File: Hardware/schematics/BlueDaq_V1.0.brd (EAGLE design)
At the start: 67 x 72 mm, 72 parts, among them IC1 MEGA8-AI, Q1 MMBT2222, Q2 MMBT2222, Q3 MMBT2222, Q4 MMBT2222, U1 MCP73831, U2 TPS61200, U3 BME280, U4 MIC5225-3.3, U5 MIC5219 5V, X1 USB-MICROB, X2 3.5mm, X4 3.5mm, Y1 16 mhz

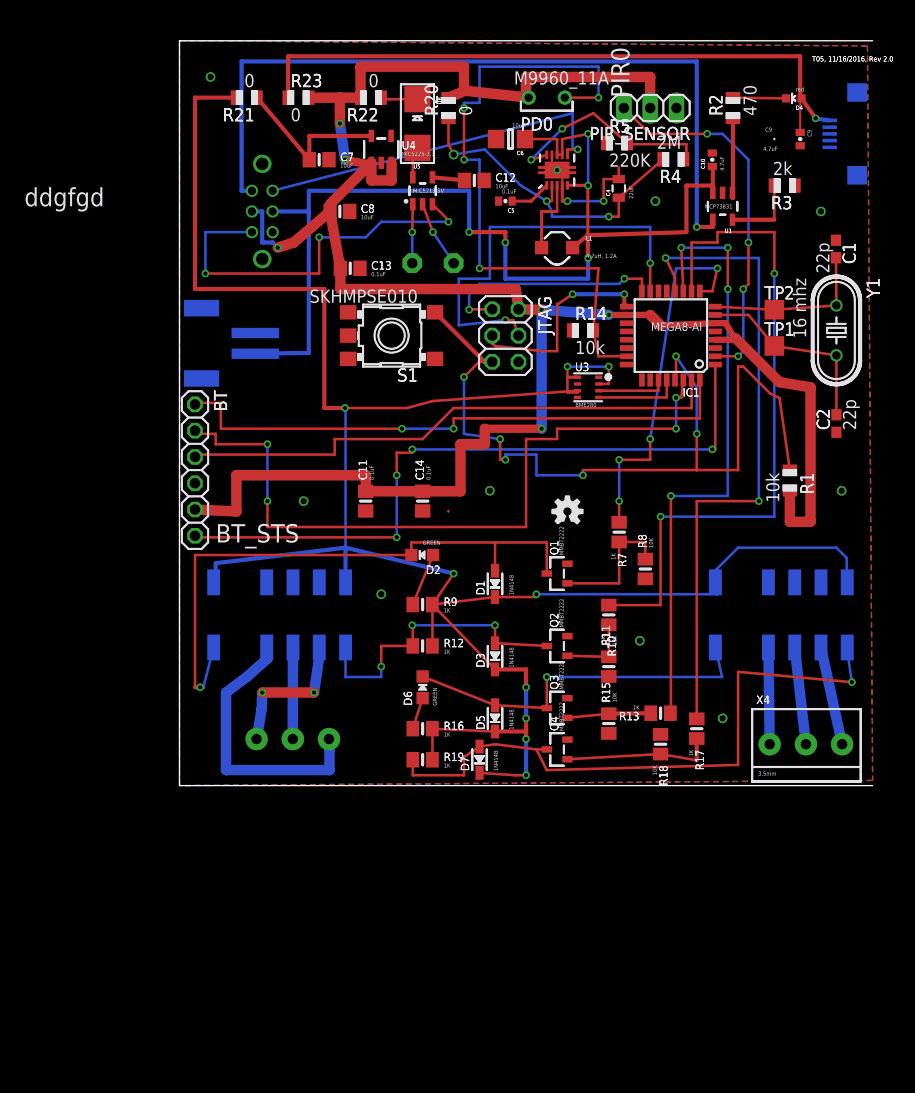
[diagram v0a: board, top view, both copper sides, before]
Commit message: cleaned up traces a little
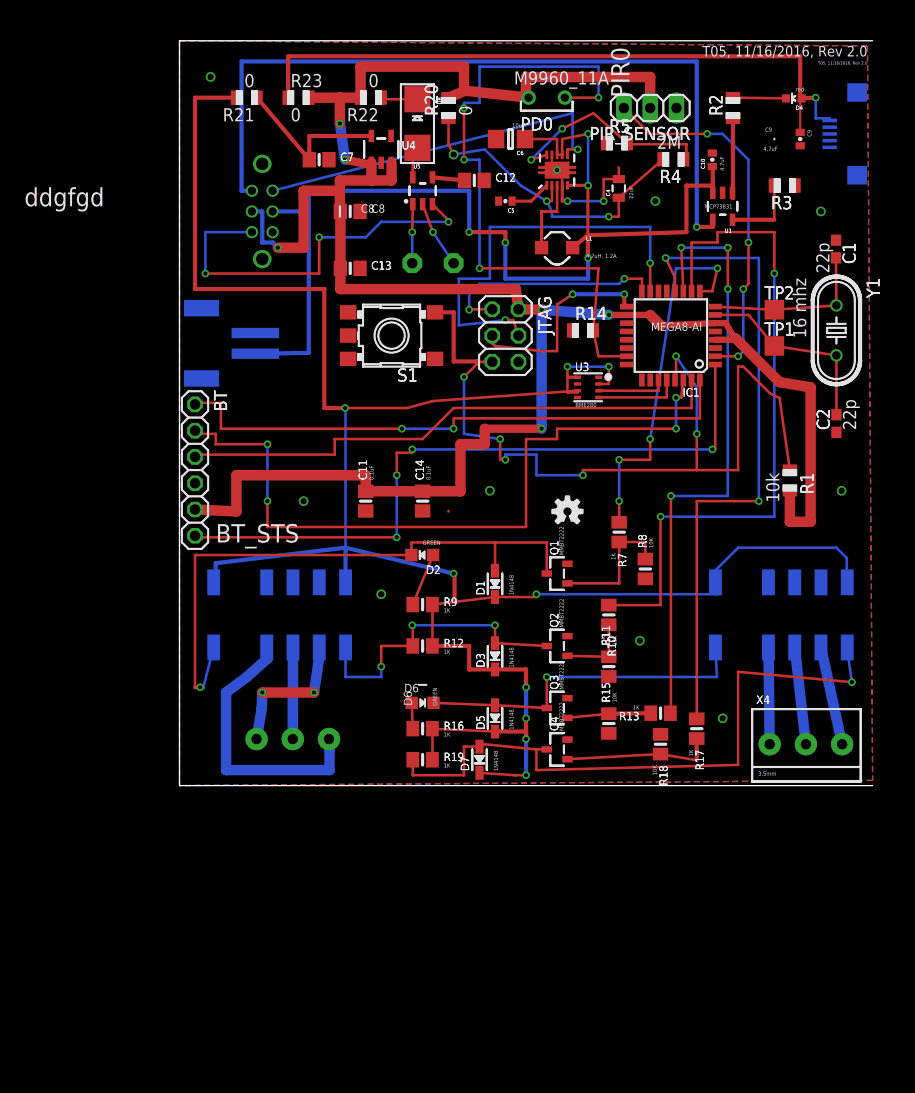
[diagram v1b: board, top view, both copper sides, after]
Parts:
- moved D6 1.50 mm to (23.0, 8.00), turned to 270 degrees
- moved C8 1.00 mm to (16.0, 55.5)
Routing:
- net VCC: track 212.1 -> 217.0 mm
- net RESET_PIN: track 84.0 -> 86.3 mm
- net N$7: track 35.4 -> 33.3 mm
- net N$12: track 60.8 -> 62.3 mm
- net 3.3V: track 218.8 -> 217.7 mm
- net N$23: track 64.7 -> 65.9 mm
- net N$9: track 3.10 -> 2.50 mm
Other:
- board text removed: "220K"
- board text removed: "2k"
- board text removed: "470"
- board text removed: "MIC5219 5V"
- board text removed: "MIC5225-3.3"
- board text removed: "R21"
- board text removed: "R22"
- board text removed: "R23"
- board text removed: "SKHMPSE010"

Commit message: lots of changes
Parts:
- removed S2: (no value), SparkFun-Electromechanical:EG2211
- added C15: 10uF, microbuilder:0805-NO@1
- added C3: 0.1uF, microbuilder:0805-NO@1
- added D10: (no value), adafruit:SMADIODE
- added R6: 4.7k, adafruit:R0805
- C12: value 10uF -> .1uF
- C13: value 0.1uF -> 10uF
- R23: value 0 -> 4.7k
- R4: value 2M -> 1.7M
- R5: value 220K -> 180K
- moved R23 90.5 mm to (-14.0, -20.5)
- moved C13 80.3 mm to (-14.0, -24.5)
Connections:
- removed net EN_5V: S2.P1-TB, U5.3
- removed net EN_BC: S2.P2-TA, U2.6
- removed net V_CHRG: S2.P1-TA, U1.4
- new net N$20: D10.A, R20.2
- new net N$36: C11.2, IC1.20
- net 3.3V: now also R23.2, R6.2
- net GND: now also C15.2, C3.1; no longer C13.2
- net N$15: now also C13.1, U5.3
- net N$16: now also C13.2
- net N$23: now also U1.4; no longer R23.1
- net N$5: now also C15.1
- net SCL: now also R6.1
- net SDA: now also R23.1
- net VBATT: now also U2.6; no longer S2.P2
- net VCC: now also C3.2, D10.C; no longer C11.2, C13.1, R20.2, R23.2, S2.P1
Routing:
- net V_CHRG: track 75.7 -> 0.00 mm, vias 1 -> 0
- net EN_5V: track 38.5 -> 0.00 mm, vias 3 -> 0
- net EN_BC: track 35.5 -> 0.00 mm, vias 1 -> 0
- net VCC: track 217.0 -> 192.8 mm
- net N$14: track 8.20 -> 0.00 mm
- net N$23: track 65.9 -> 61.9 mm
- net VBATT: track 107.9 -> 104.4 mm

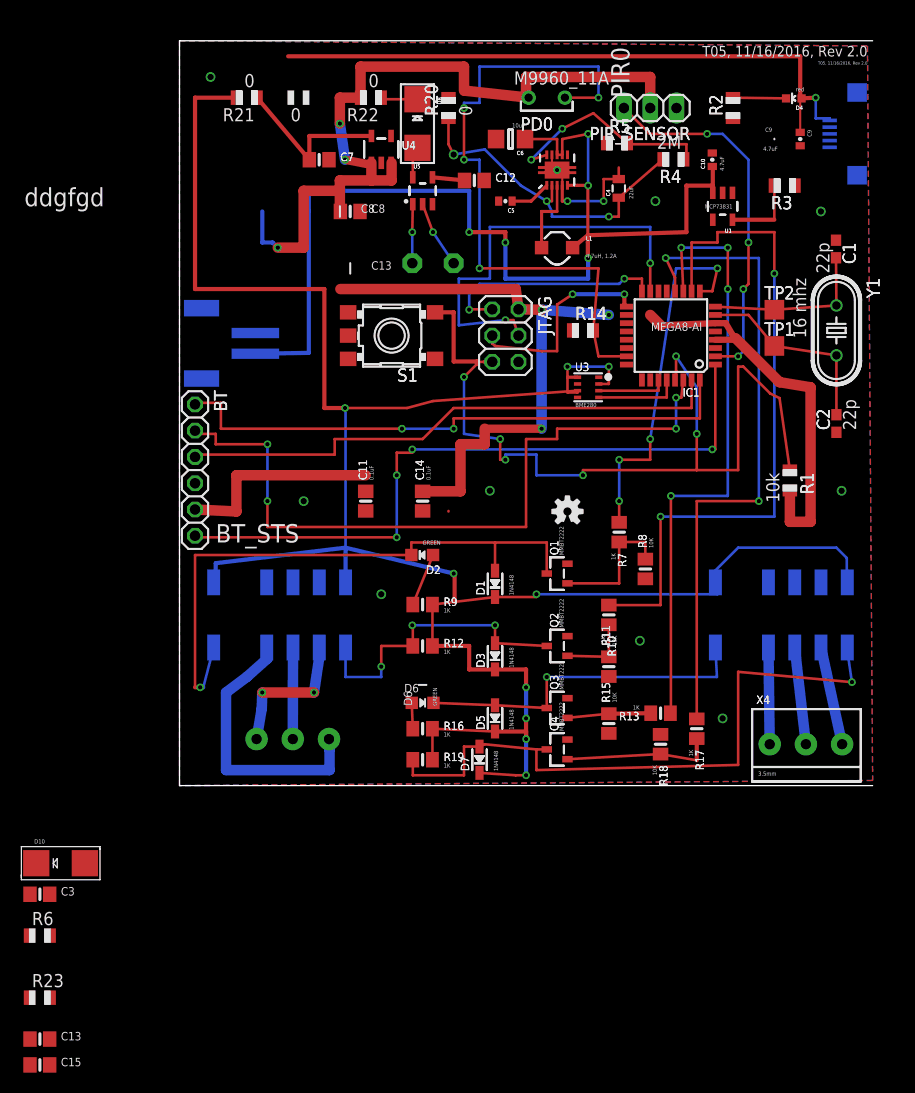
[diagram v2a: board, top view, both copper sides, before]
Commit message: placed new things, still need to do more routing
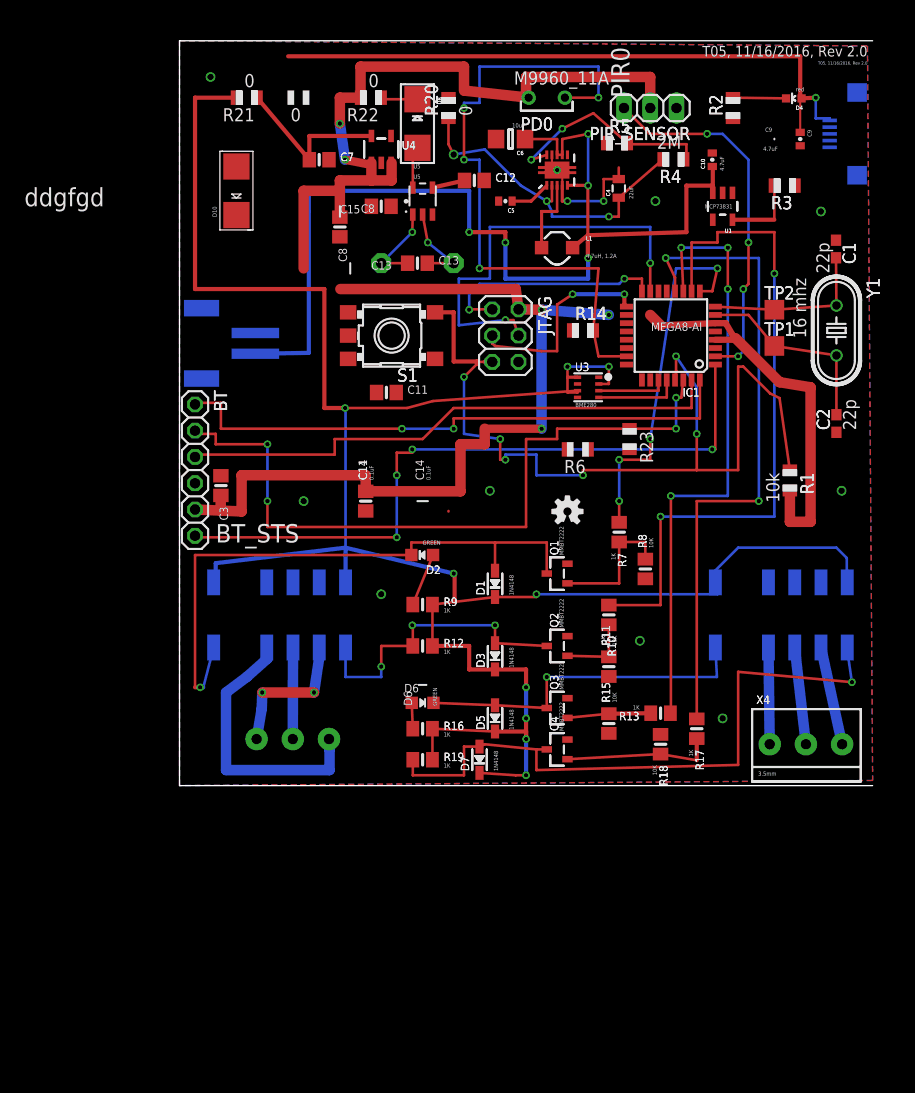
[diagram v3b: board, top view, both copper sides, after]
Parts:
- moved C15 89.3 mm to (19.0, 56.0), turned to 180 degrees
- moved C13 83.4 mm to (22.5, 50.5)
- moved R23 78.5 mm to (43.0, 33.5), turned to 270 degrees
- moved R6 70.1 mm to (38.0, 32.5), turned to 180 degrees
- moved D10 67.2 mm to (5.00, 57.5), turned to 90 degrees
- moved C3 43.2 mm to (3.50, 29.0), turned to 270 degrees
- moved C11 10.7 mm to (19.5, 38.0), turned to 0 degrees
- moved C14 5.50 mm to (17.5, 27.5)
- moved +9V 3.00 mm to (19.0, 50.5)
- moved C8 1.80 mm to (15.0, 54.0), turned to 270 degrees
- moved U5 1.00 mm to (23.0, 56.5)
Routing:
- net VCC: track 192.8 -> 196.6 mm, vias 6 -> 5
- net N$15: track 5.70 -> 8.49 mm
- net N$16: track 6.48 -> 8.50 mm
- net N$5: track 3.30 -> 4.30 mm

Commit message: more routed
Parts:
- moved R20 18.1 mm to (7.50, 67.0), turned to 270 degrees
- moved R21 6.50 mm to (3.50, 60.5)
- moved R6 6.50 mm to (35.5, 38.5), turned to 90 degrees
- moved R23 4.53 mm to (42.5, 38.0), turned to 90 degrees
- moved D10 3.91 mm to (7.50, 60.5)
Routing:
- net N$23: track 61.9 -> 8.33 mm
- net VOUT: track 32.1 -> 53.9 mm
- net VCC: track 196.6 -> 208.7 mm
- net SCL: track 8.26 -> 16.3 mm, vias 0 -> 2
- net 3.3V: track 217.7 -> 211.5 mm, vias 9 -> 7
- net N$20: track 0.00 -> 3.15 mm
- net SDA: track 6.81 -> 8.95 mm
- net BT_RX: track 70.5 -> 71.2 mm
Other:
- board text removed: "ddgfgd"

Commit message: All traces are routed
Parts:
- moved U$22 22.5 mm to (18.0, 38.5)
- moved R23 12.5 mm to (36.5, 27.0), turned to 270 degrees
- moved C11 9.50 mm to (29.0, 38.0)
- turned R14 to 180 degrees
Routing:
- net N$36: track 0.00 -> 46.9 mm, vias 0 -> 7
- net SDA: track 8.95 -> 32.8 mm, vias 0 -> 2
- net N$23: track 8.33 -> 31.7 mm, vias 1 -> 3
- net 3.3V: track 211.5 -> 224.7 mm, vias 7 -> 8
- net N$15: track 8.49 -> 20.6 mm
- net GND: track 12.7 -> 20.7 mm, vias 3 -> 5
- net N$14: track 0.00 -> 7.25 mm
- net VCC: track 208.7 -> 213.1 mm
- net N$5: track 4.30 -> 8.20 mm
- net PIR0: track 35.7 -> 38.7 mm
- net N$1: track 63.0 -> 65.9 mm
- net SCL: track 16.3 -> 14.0 mm, vias 2 -> 0
- net BT_STS: track 67.1 -> 69.3 mm
- net VBATT: track 104.4 -> 105.9 mm

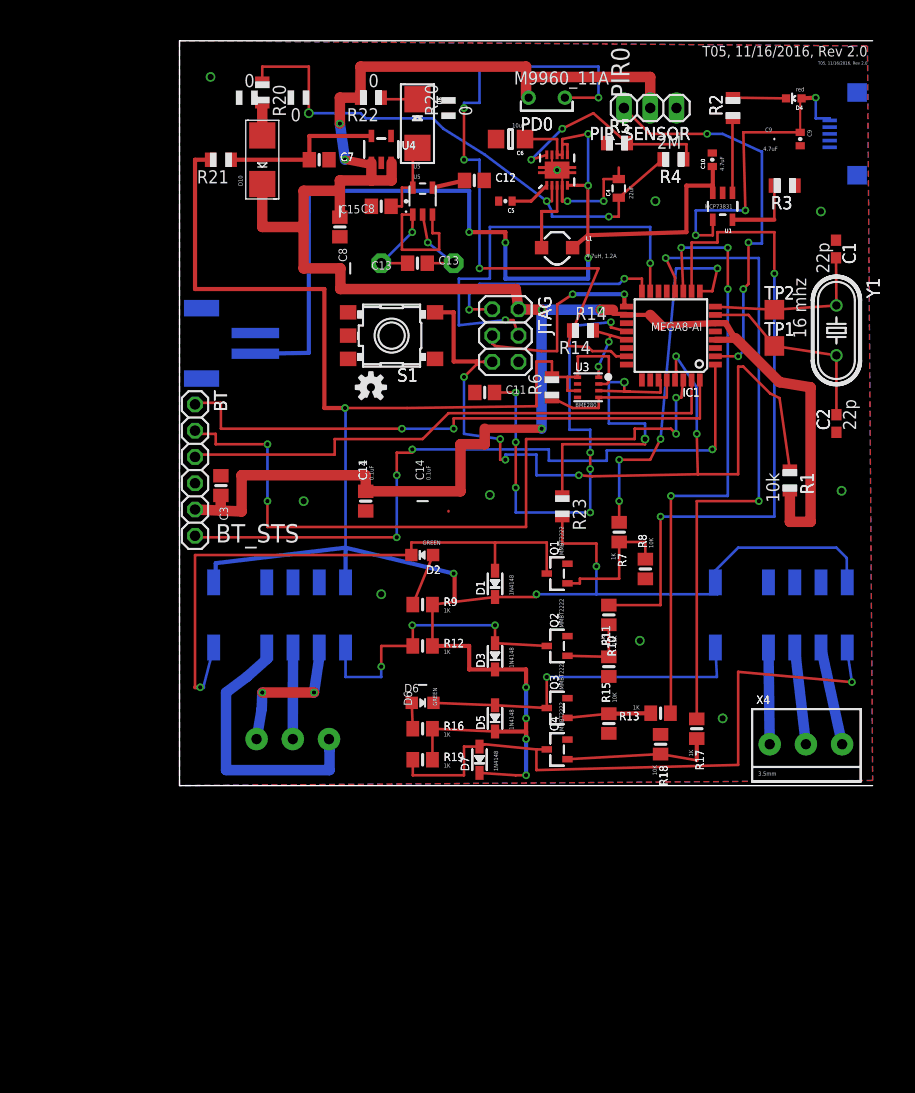
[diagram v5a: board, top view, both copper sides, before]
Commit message: fixed silk
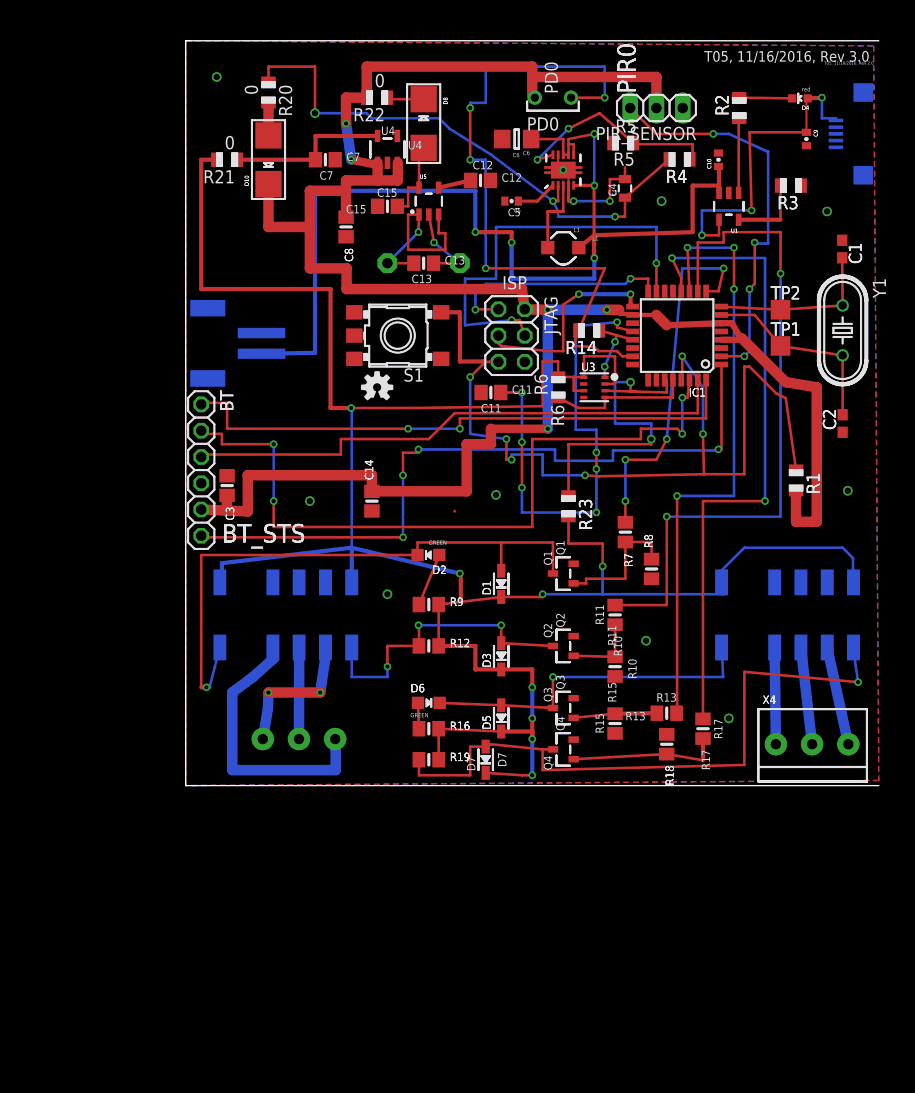
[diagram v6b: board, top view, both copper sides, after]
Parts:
- moved +9V 0.60 mm to (19.6, 50.5)
- moved -9V 0.60 mm to (26.6, 50.5)
- moved C1 0.60 mm to (63.6, 51.9)
- moved C10 0.60 mm to (51.6, 60.5)
- moved C11 0.60 mm to (29.6, 38.0)
- moved C12 0.60 mm to (28.6, 58.5)
- moved C13 0.60 mm to (23.1, 50.5)
- moved C14 0.60 mm to (18.1, 27.5)
- moved C15 0.60 mm to (19.6, 56.0)
- moved C2 0.60 mm to (63.6, 35.0)
- moved C4 0.60 mm to (42.6, 57.7)
- moved C5 0.60 mm to (31.6, 56.5)
- moved C6 0.60 mm to (32.1, 62.5)
- moved C9 0.60 mm to (60.1, 62.5)
- moved D1 0.60 mm to (30.6, 19.5)
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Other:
- board text added: "C15"
- board text added: "C3"
- board text added: "D10"
- board text added: "ISP"
- board text added: "R23"
- board text added: "R6"
- board text added: "T05, 11/16/2016, Rev 3.0"
- board text removed: "0.1uF"
- board text removed: "10K"
- board text removed: "10k"
- board text removed: "10uF"
- board text removed: "16 mhz"
- board text removed: "1K"
- board text removed: "1N4148"
- board text removed: "22p"
- board text removed: "22uF"
- board text removed: "2M"
- board text removed: "3.5mm"
- board text removed: "4.7uF"
- board text removed: "4.7uH, 1.2A"
- board text removed: "BME280"
- board text removed: "JTAG"
- board text removed: "M9960_11A"
- board text removed: "MCP73831"
- board text removed: "MEGA8-AI"
- board text removed: "MMBT2222"
- board text removed: "PIR_SENSOR"
- board text removed: "R20"
- board text removed: "S1"
- board text removed: "Y1"
